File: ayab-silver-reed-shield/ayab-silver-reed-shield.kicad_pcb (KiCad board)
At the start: 2 copper layers, 68.6 x 53.3 mm, 8 parts, among them J1 Power, J2 Digital/PWM, J3 Analog, J4 Digital/PWM

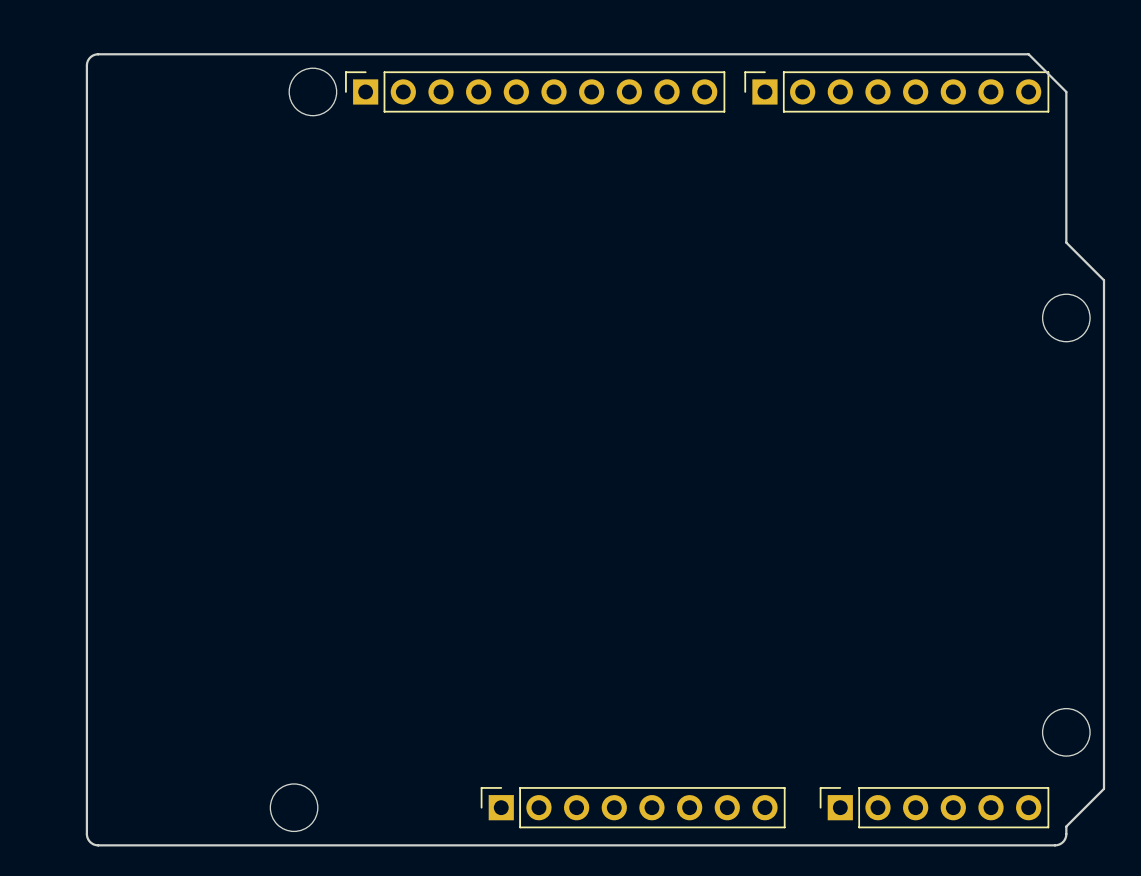
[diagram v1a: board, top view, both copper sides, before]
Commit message: Add footprints
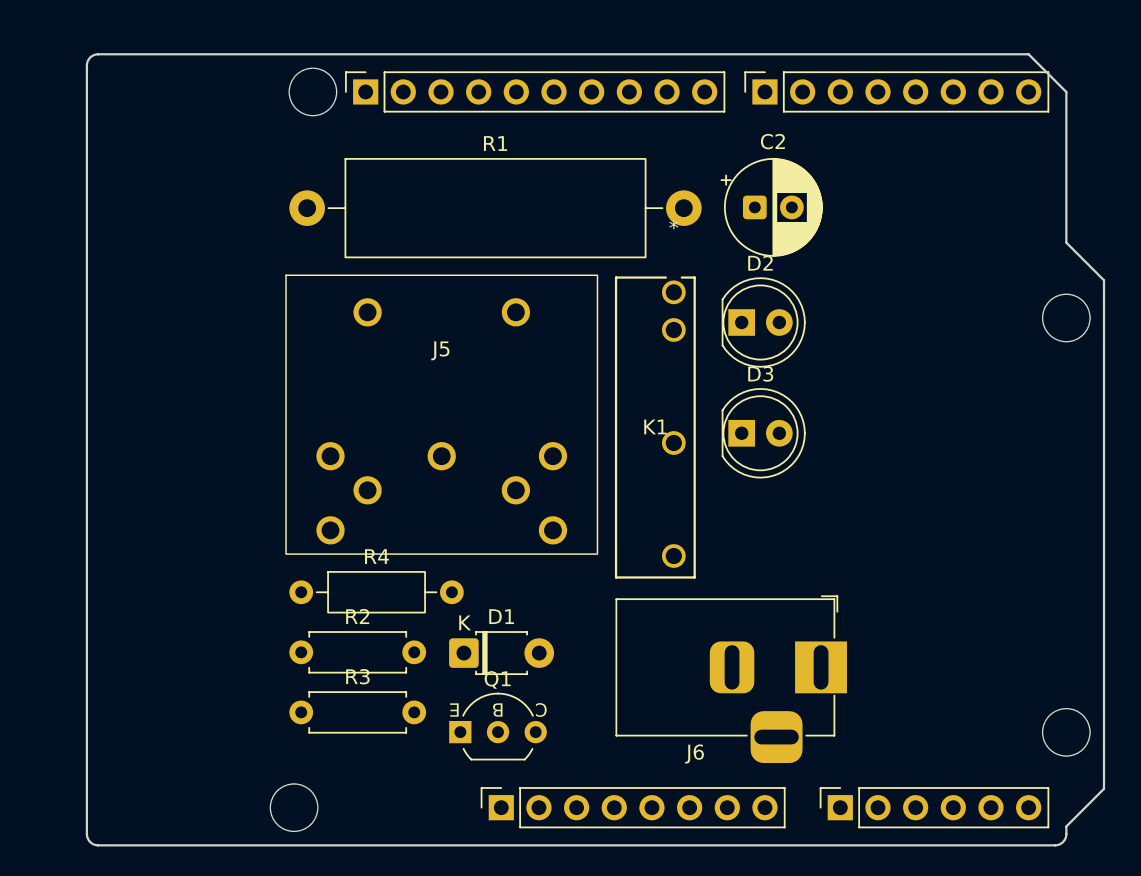
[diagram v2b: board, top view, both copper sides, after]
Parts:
- added C2: 100u, Capacitor_THT:CP_Radial_D6.3mm_P2.50mm, F.Cu at (145.0, 57.0)
- added D1: D, Diode_THT:D_T-1_P5.08mm_Horizontal, F.Cu at (125.4, 87.0)
- added D2: LED, LED_THT:LED_D5.0mm, F.Cu at (144.2, 64.7)
- added D3: LED, LED_THT:LED_D5.0mm, F.Cu at (144.2, 72.2)
- added J5: DIN-7, Locals:DIN-704-M10, F.Cu at (123.9, 71.0)
- added J6: Barrel_Jack, Connector_BarrelJack:BarrelJack_Horizontal, F.Cu at (149.5, 88.0)
- added K1: Relay_SPST-NO, Locals:RELAY_G6DN-1A_OMR, F.Cu at (139.6, 62.7)
- added Q1: 2N2222A-TO92, PCM_Package_TO_SOT_THT_AKL:TO-92_Inline_Wide_EBC, F.Cu at (125.2, 92.4)
- added R1: 10, Resistor_THT:R_Axial_Power_L20.0mm_W6.4mm_P25.40mm, F.Cu at (114.8, 57.0)
- added R2: 1K, Resistor_THT:R_Axial_DIN0207_L6.3mm_D2.5mm_P7.62mm_Horizontal, F.Cu at (114.5, 87.0)
- added R3: 1K, Resistor_THT:R_Axial_DIN0207_L6.3mm_D2.5mm_P7.62mm_Horizontal, F.Cu at (114.5, 91.0)
- added R4: 1K, Resistor_THT:R_Axial_DIN0207_L6.3mm_D2.5mm_P10.16mm_Horizontal, F.Cu at (114.5, 82.9)

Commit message: Add PCB board design
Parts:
- C2: footprint Capacitor_THT:CP_Radial_D6.3mm_P2.50mm -> Locals:CP_6.3x11mm_horiz-R
- J1, J4: footprint Connector_PinSocket_2.54mm:PinSocket_1x08_P2.54mm_Vertical -> Connector_PinHeader_2.54mm:PinHeader_1x08_P2.54mm_Vertical; moved to B.Cu
- J2: footprint Connector_PinSocket_2.54mm:PinSocket_1x10_P2.54mm_Vertical -> Connector_PinHeader_2.54mm:PinHeader_1x10_P2.54mm_Vertical; moved to B.Cu
- J3: footprint Connector_PinSocket_2.54mm:PinSocket_1x06_P2.54mm_Vertical -> Connector_PinHeader_2.54mm:PinHeader_1x06_P2.54mm_Vertical; moved to B.Cu
- R2, R3: footprint Resistor_THT:R_Axial_DIN0207_L6.3mm_D2.5mm_P7.62mm_Horizontal -> Resistor_THT:R_Axial_DIN0207_L6.3mm_D2.5mm_P2.54mm_Vertical
- R4: footprint Resistor_THT:R_Axial_DIN0207_L6.3mm_D2.5mm_P10.16mm_Horizontal -> Resistor_THT:R_Axial_DIN0207_L6.3mm_D2.5mm_P2.54mm_Vertical
- moved D3 47.0 mm to (102.2, 51.0)
- moved J6 40.3 mm to (110.0, 80.0)
- moved C2 38.0 mm to (124.6, 89.0)
- moved Q1 36.1 mm to (121.6, 56.5), turned to -90 degrees
- moved J5 35.8 mm to (159.1, 77.5), turned to -90 degrees
- moved R3 35.2 mm to (129.0, 59.0)
- moved R4 33.2 mm to (110.0, 50.0), turned to -90 degrees
- moved D2 26.0 mm to (118.5, 69.0), turned to -90 degrees
- moved D1 25.9 mm to (114.5, 63.5), turned to 90 degrees
- moved R1 23.1 mm to (117.3, 80.0)
- moved R2 15.7 mm to (112.0, 71.5), turned to 90 degrees
- moved K1 13.3 mm to (127.3, 68.0), turned to 90 degrees
- turned J1 to -90 degrees
- turned J2 to -90 degrees
- turned J3 to -90 degrees
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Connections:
- J2 pad 1: /SCL/A5 -> /A5
- J2 pad 2: /SDA/A4 -> /A4
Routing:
- net GND: track 0.00 -> 149.8 mm
- net +5V: track 0.00 -> 91.3 mm
- net /2: track 0.00 -> 40.9 mm
- net /*5: track 0.00 -> 39.6 mm
- net Net-(C2-Pad2): track 0.00 -> 35.9 mm
- net /*3: track 0.00 -> 33.4 mm
- net Net-(D1-A): track 0.00 -> 27.2 mm
- net /*6: track 0.00 -> 25.7 mm
- net /4: track 0.00 -> 22.2 mm
- net Net-(C2-Pad1): track 0.00 -> 20.9 mm
- net Net-(J5-Pad6): track 0.00 -> 19.6 mm
- net /7: track 0.00 -> 18.3 mm
- net Net-(Q1-B): track 0.00 -> 7.32 mm
- net Net-(D2-A): track 0.00 -> 6.52 mm
- net Net-(D3-A): track 0.00 -> 5.65 mm

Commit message: Add mass plan
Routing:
- added copper zone on B.Cu, net GND
- added copper zone on F.Cu, net GND
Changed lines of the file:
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@@
 		(net 35)
+	)
+	(zone
+		(net 1)
+		(net_name "GND")
+		(layers "F.Cu" "B.Cu")
+		(hatch edge 0.5)
+		(connect_pads
+			(clearance 0.508)
+		)
+		(min_thickness 0.25)
+		(filled_areas_thickness no)
+		(fill yes
+			(thermal_gap 0.5)
+			(thermal_bridge_width 0.5)
+		)
+		(polygon
+			(pts
+				(xy 99 46) (xy 99 100) (xy 169 100) (xy 168 46)
+			)
+		)
 	)
 	(embedded_fonts no)

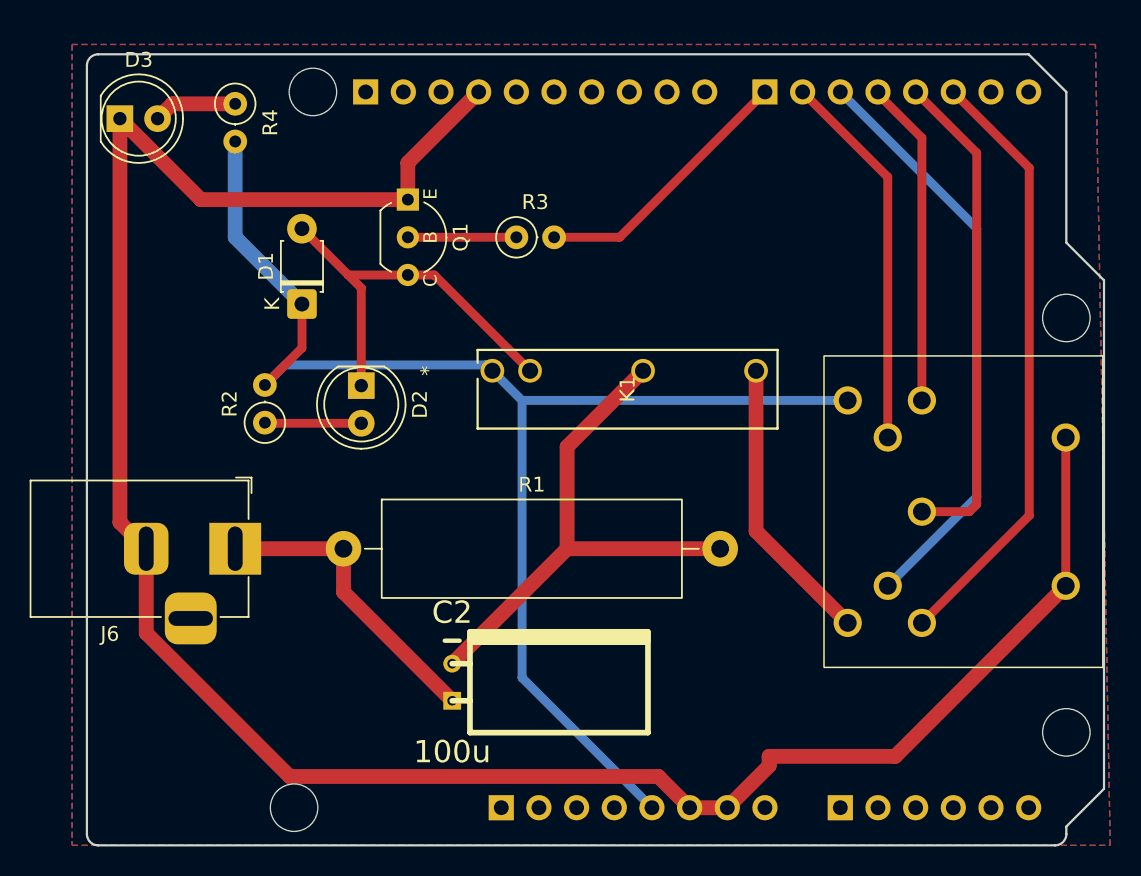
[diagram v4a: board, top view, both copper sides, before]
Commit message: Add mass plan without gnd links
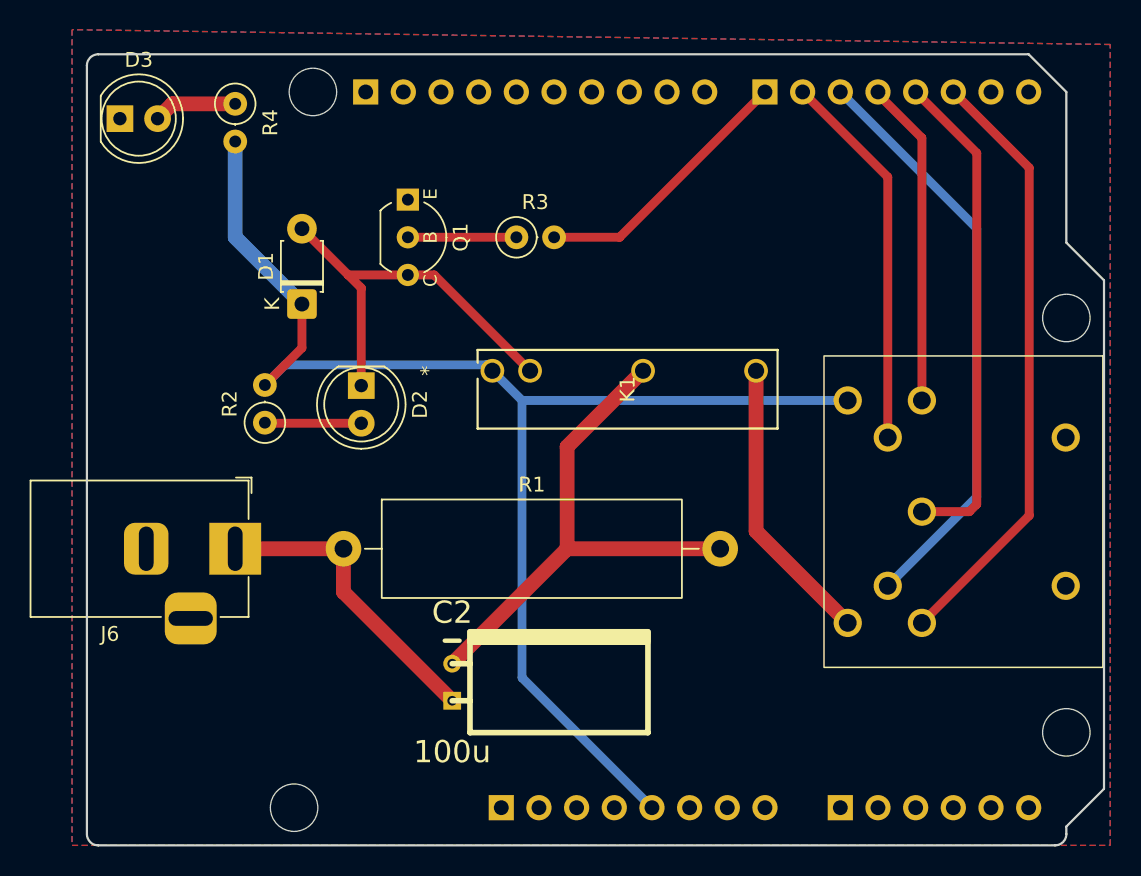
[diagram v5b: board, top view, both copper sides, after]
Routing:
- net GND: track 149.8 -> 0.00 mm
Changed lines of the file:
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@@
-	)
-	(segment
-		(start 102.225 51)
-		(end 102.225 78.225)
-		(width 1)
-		(layer "F.Cu")
-		(net 1)
-	)
-	(segment
-		(start 102.225 51)
-		(end 107.685 56.46)
-		(width 1)
-		(layer "F.Cu")
-		(net 1)
-	)
-	(segment
-		(start 113.672902 95.359)
-		(end 138.539 95.359)
-		(width 1)
-		(layer "F.Cu")
-		(net 1)
-	)
-	(segment
-		(start 121.64 53.976)
-		(end 126.416 49.2)
-		(width 1)
-		(layer "F.Cu")
-		(net 1)
-	)
-	(segment
-		(start 121.64 56.46)
-		(end 121.64 53.976)
-		(width 1)
-		(layer "F.Cu")
-		(net 1)
-	)
-	(segment
-		(start 166 72.5)
-		(end 166 82.5)
-		(width 0.6)
-		(layer "F.Cu")
-		(net 1)
-	)
-	(segment
-		(start 104 85.686098)
-		(end 113.672902 95.359)
-		(width 1)
-		(layer "F.Cu")
-		(net 1)
-	)
-	(segment
-		(start 166 82.5)
-		(end 154.5 94)
-		(width 1)
-		(layer "F.Cu")
-		(net 1)
-	)
-	(segment
-		(start 154.5 94)
-		(end 146 94)
-		(width 1)
-		(layer "F.Cu")
-		(net 1)
-	)
-	(segment
-		(start 104 80)
-		(end 104 85.686098)
-		(width 1)
-		(layer "F.Cu")
-		(net 1)
-	)
-	(segment
-		(start 146 94)
-		(end 146 94.64)
-		(width 1)
-		(layer "F.Cu")
-		(net 1)
-	)
-	(segment
-		(start 107.685 56.46)
-		(end 121.64 56.46)
-		(width 1)
-		(layer "F.Cu")
-		(net 1)
-	)
-	(segment
-		(start 102.225 78.225)
-		(end 104 80)
-		(width 1)
-		(layer "F.Cu")
-		(net 1)
-	)
-	(segment
-		(start 138.539 95.359)
-		(end 140.64 97.46)
-		(width 1)
-		(layer "F.Cu")
-		(net 1)
-	)
-	(segment
-		(start 140.64 97.46)
-		(end 143.18 97.46)
-		(width 1)
-		(layer "F.Cu")
-		(net 1)
-	)
-	(segment
-		(start 146 94.64)
-		(end 143.18 97.46)
-		(width 1)
-		(layer "F.Cu")
-		(net 1)
 	)
 	(segment
@@
 		(polygon
 			(pts
-				(xy 99 46) (xy 99 100) (xy 169 100) (xy 168 46)
+				(xy 99 45) (xy 99 100) (xy 169 100) (xy 169 46)
 			)
 		)

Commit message: Increase 16V traces to 2mm
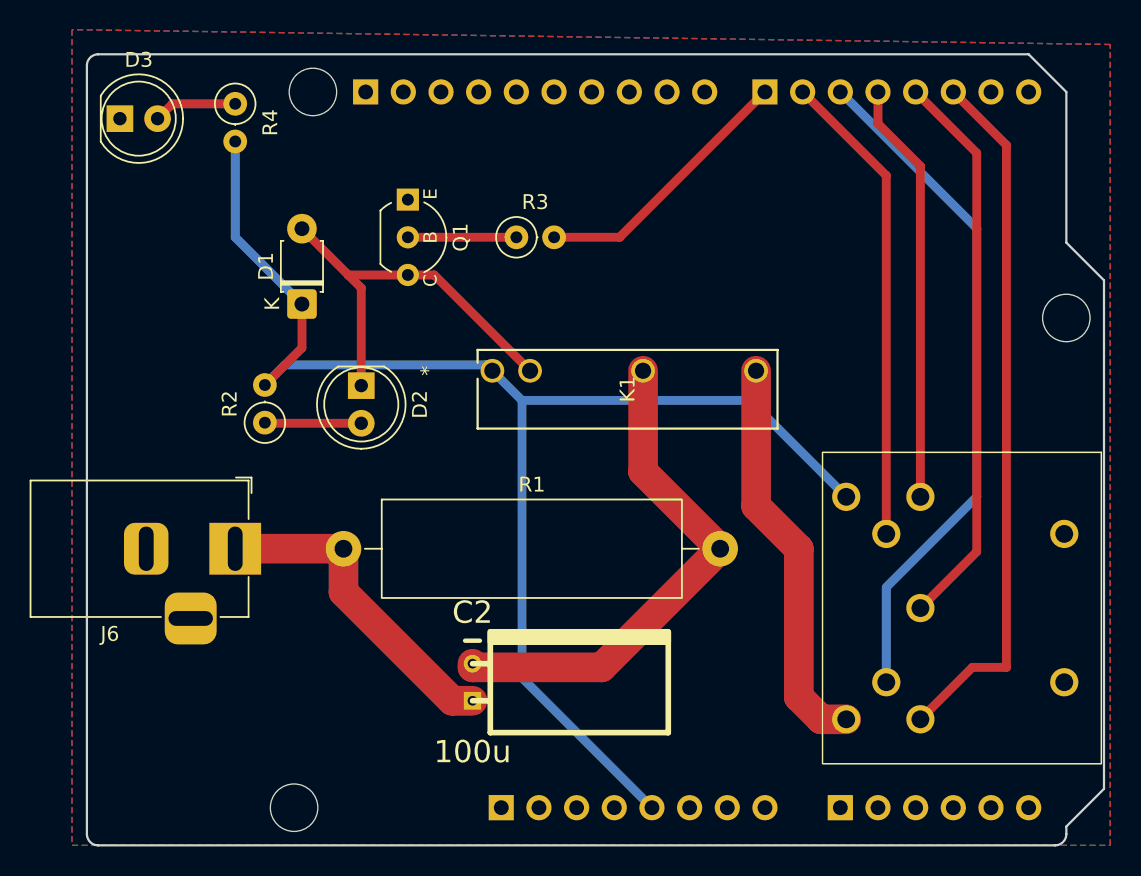
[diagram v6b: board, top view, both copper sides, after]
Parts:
- removed MH4: MountingHole_3.2mm, Arduino_MountingHole:MountingHole_3.2mm
- moved J5 6.50 mm to (159.0, 84.0)
- moved C2 1.37 mm to (126.0, 89.0)
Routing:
- net Net-(J5-Pad6): track 19.6 -> 27.0 mm
- net /2: track 40.9 -> 47.5 mm
- net /*5: track 39.6 -> 46.1 mm
- net /*6: track 25.7 -> 32.1 mm
- net /4: track 22.2 -> 28.6 mm
- net /*3: track 33.4 -> 38.1 mm
- net +5V: track 91.3 -> 93.9 mm
- net Net-(C2-Pad1): track 20.9 -> 22.3 mm
- net Net-(C2-Pad2): track 35.9 -> 34.9 mm

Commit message: Add text
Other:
- board text added: "AYAB - SilverReed interface"
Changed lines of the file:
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@@
 		(layer "Edge.Cuts")
+	)
+	(gr_text "AYAB - SilverReed interface\n"
+		(at 143 57.63 0)
+		(layer "F.SilkS")
+		(effects
+			(font
+				(size 1 1)
+				(thickness 0.15)
+			)
+			(justify left bottom)
+		)
 	)
 	(gr_text "ICSP"
@@
 	)
 	(segment
+		(start 124.62975 90.25)
+		(end 126 90.25)
+		(width 2)
+		(layer "F.Cu")
+		(net 29)
+	)
+	(segment
+		(start 117.3 80)
+		(end 117.3 82.92025)
+		(width 2)
+		(layer "F.Cu")
+		(net 29)
+	)
+	(segment
 		(start 117.3 82.92025)
 		(end 124.62975 90.25)
@@
 	)
 	(segment
-		(start 124.62975 90.25)
-		(end 126 90.25)
-		(width 2)
-		(layer "F.Cu")
-		(net 29)
-	)
-	(segment
-		(start 117.3 80)
-		(end 117.3 82.92025)
-		(width 2)
-		(layer "F.Cu")
-		(net 29)
-	)
-	(segment
 		(start 117.3 80)
 		(end 117 80)
@@
 	)
 	(segment
-		(start 134.7 88)
-		(end 142.7 80)
-		(width 2)
-		(layer "F.Cu")
-		(net 30)
-	)
-	(segment
 		(start 137.5 68)
 		(end 137.5 74.8)
@@
 	)
 	(segment
-		(start 126 87.75)
-		(end 126 88)
+		(start 133.75 80)
+		(end 126 87.75)
 		(width 2)
 		(layer "F.Cu")
@@
 	)
 	(segment
-		(start 126 88)
-		(end 134.7 88)
-		(width 2)
-		(layer "F.Cu")
+		(start 142.7 80)
+		(end 133.75 80)
+		(width 2)
+		(layer "F.Cu")
